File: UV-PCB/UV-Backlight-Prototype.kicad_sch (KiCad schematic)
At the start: 59 parts, among them J1 Conn_02x08_Odd_Even

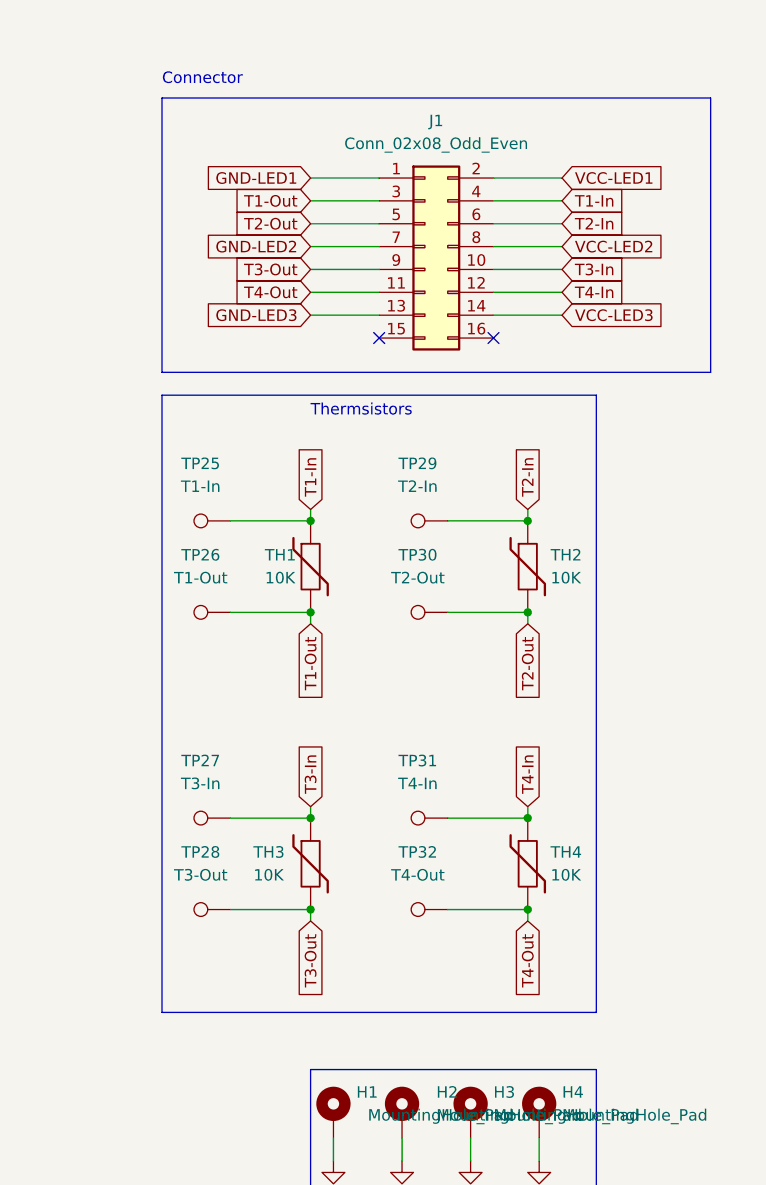
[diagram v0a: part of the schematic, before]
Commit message: UV Backlight and PS
Power Supply creation
V2 for backlight, removed thermsistors
Changed the connector, simplified the board
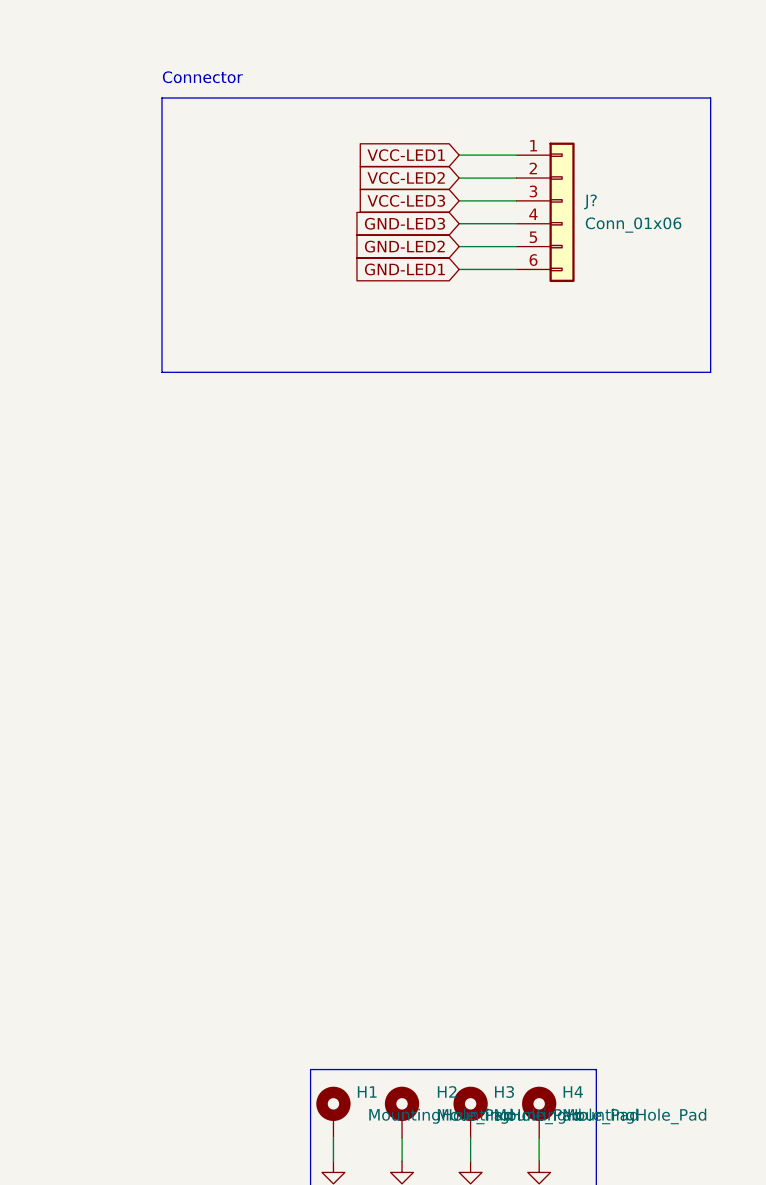
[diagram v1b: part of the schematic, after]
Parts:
- removed J1: Conn_02x08_Odd_Even, Connector_IDC:IDC-Header_2x08_P2.54mm_Vertical, symbol Connector_Generic:Conn_02x08_Odd_Even
- removed TH1, TH2, TH3, TH4: 10K, Resistor_SMD:R_1206_3216Metric_Pad1.30x1.75mm_HandSolder, symbol Device:Thermistor
- removed TP25: T1-In, TestPoint:TestPoint_Keystone_5000-5004_Miniature, symbol Connector:TestPoint
- removed TP26: T1-Out, TestPoint:TestPoint_Keystone_5000-5004_Miniature, symbol Connector:TestPoint
- removed TP27: T3-In, TestPoint:TestPoint_Keystone_5000-5004_Miniature, symbol Connector:TestPoint
- removed TP28: T3-Out, TestPoint:TestPoint_Keystone_5000-5004_Miniature, symbol Connector:TestPoint
- removed TP29: T2-In, TestPoint:TestPoint_Keystone_5000-5004_Miniature, symbol Connector:TestPoint
- removed TP30: T2-Out, TestPoint:TestPoint_Keystone_5000-5004_Miniature, symbol Connector:TestPoint
- removed TP31: T4-In, TestPoint:TestPoint_Keystone_5000-5004_Miniature, symbol Connector:TestPoint
- removed TP32: T4-Out, TestPoint:TestPoint_Keystone_5000-5004_Miniature, symbol Connector:TestPoint
- added J?: Conn_01x06, symbol Connector_Generic:Conn_01x06
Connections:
- net GND-LED1: now also J?.6 (Pin_6)
- net GND-LED2: now also J?.5 (Pin_5)
- net GND-LED3: now also J?.4 (Pin_4)
- net VCC-LED1: now also J?.1 (Pin_1)
- net VCC-LED2: now also J?.2 (Pin_2)
- net VCC-LED3: now also J?.3 (Pin_3)
- no-connect marks 2 -> 0
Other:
- note removed: "Thermsistors"

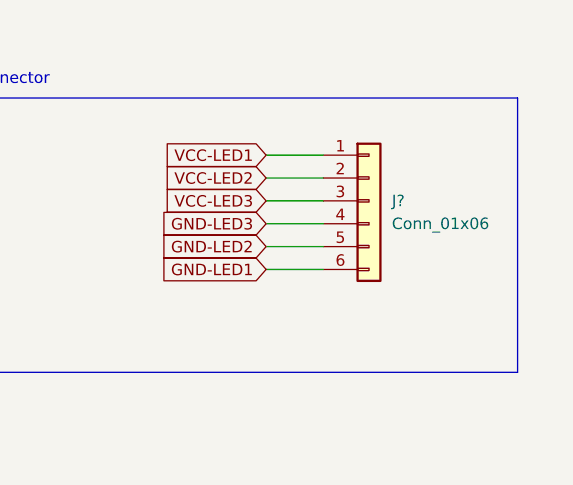
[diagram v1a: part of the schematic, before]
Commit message: Update UV-Backlight-Prototype.kicad_sch
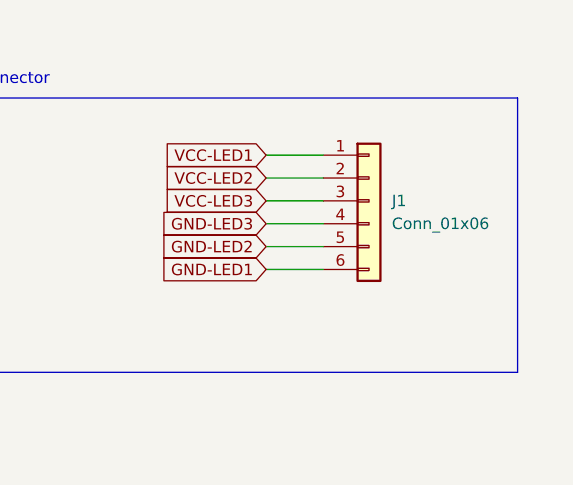
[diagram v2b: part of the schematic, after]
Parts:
- gave numbers to parts that had none: 1
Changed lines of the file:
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@@
   (symbol (lib_id "Connector_Generic:Conn_01x06") (at 257.81 35.56 0) (unit 1)
     (in_bom yes) (on_board yes) (fields_autoplaced)
-    (property "Reference" "J?" (id 0) (at 260.35 35.5599 0)
+    (property "Reference" "J1" (id 0) (at 260.35 35.5599 0)
       (effects (font (size 1.27 1.27)) (justify left))
     )
@@
     )
     (path "/821f5a43-6a49-4993-9d0f-8ed3f85ec7b9"
-      (reference "J?") (unit 1) (value "Conn_01x06") (footprint "Connector_JST:JST_XH_B6B-XH-A_1x06_P2.50mm_Vertical")
+      (reference "J1") (unit 1) (value "Conn_01x06") (footprint "Connector_JST:JST_XH_B6B-XH-A_1x06_P2.50mm_Vertical")
     )
     (path "/d72ca844-d7cd-4b05-8f47-fa9aafe60d3a"
